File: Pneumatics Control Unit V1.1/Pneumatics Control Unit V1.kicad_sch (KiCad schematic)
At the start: 43 parts

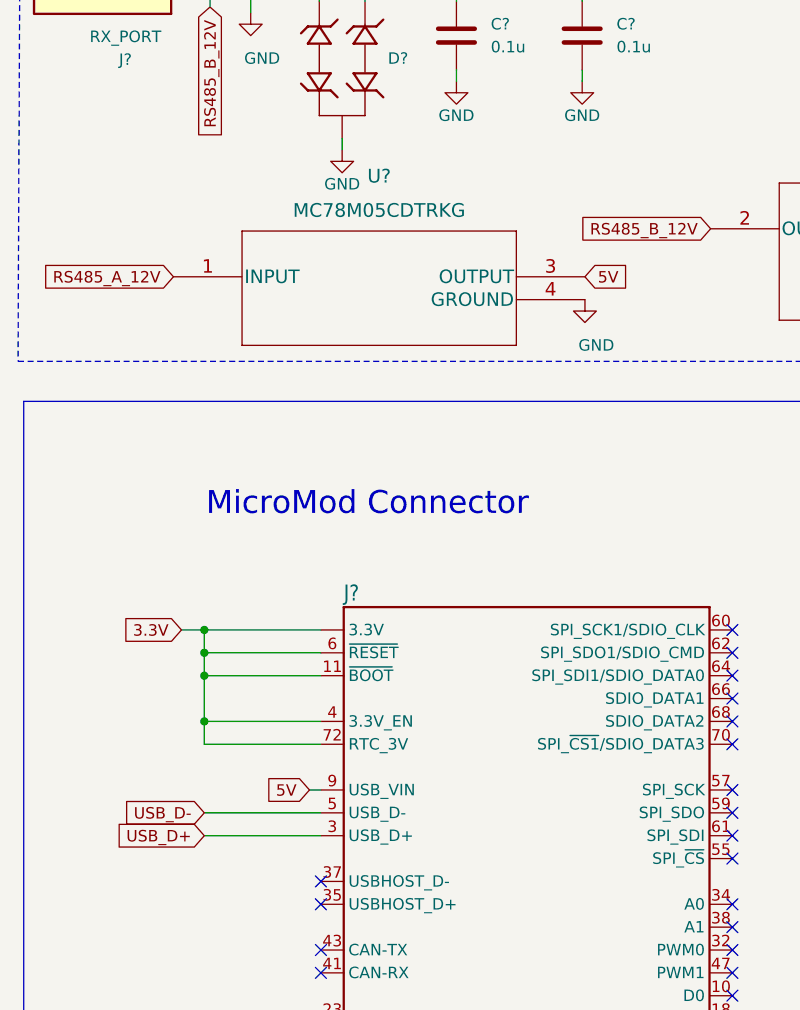
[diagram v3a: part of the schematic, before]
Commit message: Adding voltage converters
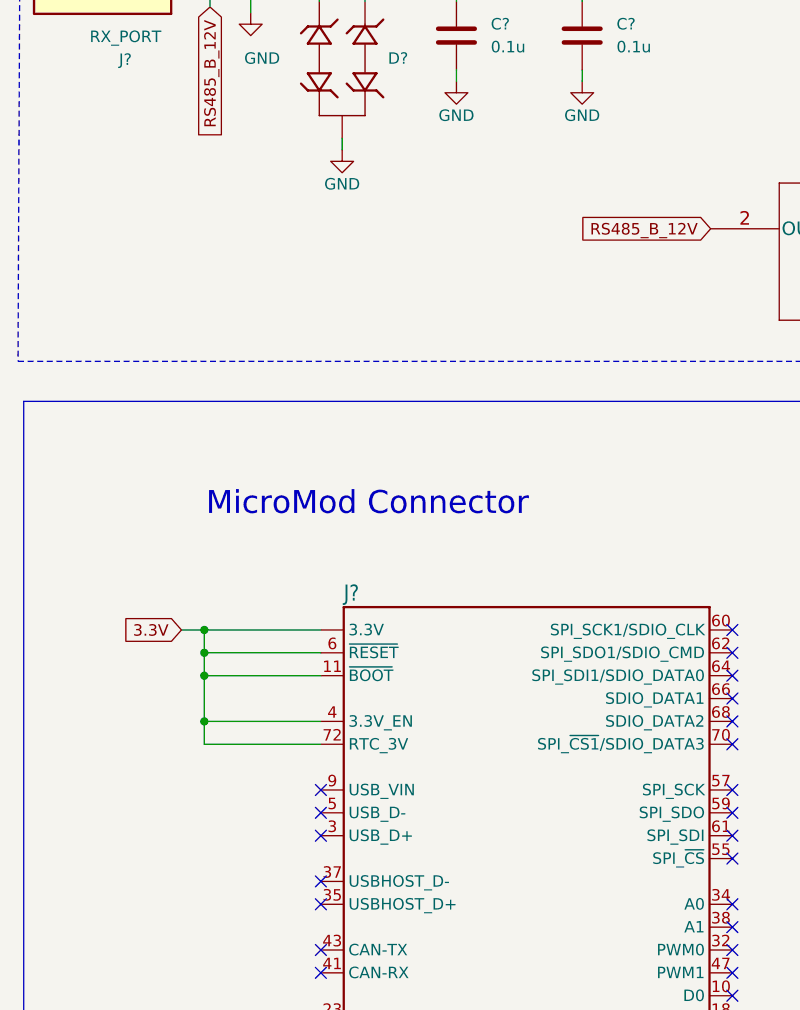
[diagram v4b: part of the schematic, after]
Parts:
- removed U?: MC78M05CDTRKG, DPAK-3_ONS, symbol 2022-03-25_21-05-18:MC78M05CDTRKG
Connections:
- net 5V: no longer names the net of J?.9 (USB_VIN)
- net USB_D+: no longer names the net of J?.3 (USB_D+)
- net USB_D-: no longer names the net of J?.5 (USB_D-)
- no-connect marks 42 -> 45
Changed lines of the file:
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@@
   (no_connect (at 97.155 236.855))
   (no_connect (at 97.155 239.395))
+  (no_connect (at 48.895 163.195))
+  (no_connect (at 48.895 165.735))
+  (no_connect (at 48.895 168.275))
   (no_connect (at 23.495 210.185))
   (no_connect (at 48.895 226.695))
@@
     (stroke (width 0) (type default) (color 0 0 0 0))
   )
-  (wire (pts (xy 35.941 168.275) (xy 48.895 168.275))
-    (stroke (width 0) (type default) (color 0 0 0 0))
-  )
   (wire (pts (xy 104.648 34.3154) (xy 99.5172 34.3154))
     (stroke (width 0) (type default) (color 0 0 0 0))
@@
     (stroke (width 0) (type default) (color 0 0 0 0))
   )
-  (wire (pts (xy 35.941 165.735) (xy 48.895 165.735))
-    (stroke (width 0) (type default) (color 0 0 0 0))
-  )
   (wire (pts (xy 295.91 88.9) (xy 321.31 88.9))
     (stroke (width 0) (type default) (color 0 0 0 0))
@@
   )
   (wire (pts (xy 250.19 52.705) (xy 242.57 52.705))
-    (stroke (width 0) (type default) (color 0 0 0 0))
-  )
-  (wire (pts (xy 47.625 163.195) (xy 48.895 163.195))
     (stroke (width 0) (type default) (color 0 0 0 0))
   )
@@
     )
   )
-  (global_label "USB_D+" (shape input) (at 35.941 168.275 180)
-    (effects (font (size 1.27 1.27)) (justify right))
-    (property "Intersheet References" "${INTERSHEET_REFS}" (id 0) (at 24.3839 168.3544 0)
-      (effects (font (size 1.27 1.27)) (justify right) hide)
-    )
-  )
   (global_label "RS485_RXD" (shape input) (at 128.778 54.61 0)
     (effects (font (size 1.27 1.27)) (justify left))
@@
     )
   )
-  (global_label "RS485_A_12V" (shape input) (at 32.512 106.172 180) (fields_autoplaced)
-    (effects (font (size 1.27 1.27)) (justify right))
-    (property "Intersheet References" "${INTERSHEET_REFS}" (id 0) (at 17.2689 106.0926 0)
-      (effects (font (size 1.27 1.27)) (justify right) hide)
-    )
-  )
   (global_label "3.3V" (shape input) (at 158.242 100.838 0) (fields_autoplaced)
     (effects (font (size 1.27 1.27)) (justify left))
@@
     )
   )
-  (global_label "5V" (shape input) (at 78.232 106.172 0) (fields_autoplaced)
-    (effects (font (size 1.27 1.27)) (justify left))
-    (property "Intersheet References" "${INTERSHEET_REFS}" (id 0) (at 83.1337 106.0926 0)
-      (effects (font (size 1.27 1.27)) (justify left) hide)
-    )
-  )
   (global_label "RS485_TXD" (shape input) (at 129.032 50.292 0)
     (effects (font (size 1.27 1.27)) (justify left))
@@
     )
   )
-  (global_label "USB_D-" (shape input) (at 35.941 165.735 180)
-    (effects (font (size 1.27 1.27)) (justify right))
-    (property "Intersheet References" "${INTERSHEET_REFS}" (id 0) (at 24.3839 165.6556 0)
-      (effects (font (size 1.27 1.27)) (justify right) hide)
-    )
-  )
   (global_label "RS485_TXD" (shape input) (at 148.4376 31.7754 0)
     (effects (font (size 1.27 1.27)) (justify left))
@@
     (effects (font (size 1.27 1.27)) (justify left))
     (property "Intersheet References" "${INTERSHEET_REFS}" (id 0) (at 81.3646 193.5956 0)
-      (effects (font (size 1.27 1.27)) (justify right) hide)
-    )
-  )
-  (global_label "5V" (shape input) (at 47.625 163.195 180) (fields_autoplaced)
-    (effects (font (size 1.27 1.27)) (justify right))
-    (property "Intersheet References" "${INTERSHEET_REFS}" (id 0) (at 42.7233 163.1156 0)
       (effects (font (size 1.27 1.27)) (justify right) hide)
     )
@@
     (pin "2")
     (pin "3")
-  )
-  (symbol (lib_id "power:GND") (at 78.232 108.712 0) (unit 1)
-    (in_bom yes) (on_board yes)
-    (property "Reference" "#PWR?" (id 0) (at 78.232 115.062 0)
-      (effects (font (size 1.27 1.27)) hide)
-    )
-    (property "Value" "GND" (id 1) (at 79.502 113.792 0))
-    (property "Footprint" "" (id 2) (at 78.232 108.712 0)
-      (effects (font (size 1.27 1.27)) hide)
-    )
-    (property "Datasheet" "" (id 3) (at 78.232 108.712 0)
-      (effects (font (size 1.27 1.27)) hide)
-    )
-    (pin "1")
   )
   (symbol (lib_id "Connector:Conn_01x02_Male") (at 260.35 28.575 180) (unit 1)
@@
     (pin "2")
   )
-  (symbol (lib_id "2022-03-25_21-05-18:MC78M05CDTRKG") (at 32.512 106.172 0) (unit 1)
-    (in_bom yes) (on_board yes) (fields_autoplaced)
-    (property "Reference" "U?" (id 0) (at 55.372 94.996 0)
-      (effects (font (size 1.524 1.524)))
-    )
-    (property "Value" "MC78M05CDTRKG" (id 1) (at 55.372 98.806 0)
-      (effects (font (size 1.524 1.524)))
-    )
-    (property "Footprint" "DPAK-3_ONS" (id 2) (at 55.372 100.076 0)
-      (effects (font (size 1.524 1.524)) hide)
-    )
-    (property "Datasheet" "" (id 3) (at 32.512 106.172 0)
-      (effects (font (size 1.524 1.524)))
-    )
-    (pin "1")
-    (pin "3")
-    (pin "4")
-  )
   (symbol (lib_id "power:GND") (at 220.98 53.975 0) (unit 1)
     (in_bom yes) (on_board yes)
@@
       (reference "#PWR?") (unit 1) (value "GND") (footprint "")
     )
-    (path "/907ee120-1742-4b9b-9a3f-9a17112149c4"
-      (reference "#PWR?") (unit 1) (value "GND") (footprint "")
-    )
     (path "/931a035c-dacd-431f-910b-def670bdc676"
       (reference "#PWR?") (unit 1) (value "GND") (footprint "")
@@
       (reference "U?") (unit 1) (value "NCP1117LPST33T3G") (footprint "SOT223-3_ONS")
     )
-    (path "/b9b54933-6106-46ac-bf2e-8b30431ef848"
-      (reference "U?") (unit 1) (value "MC78M05CDTRKG") (footprint "DPAK-3_ONS")
-    )
-  )
+  )

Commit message: Changing to net labels
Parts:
- removed D? (x7): D_TVS_x2_AAC, Package_TO_SOT_SMD:SOT-723, symbol Device:D_TVS_x2_AAC
- removed J? (x7): Conn_01x02_Male, Connector_PinSocket_2.54mm:PinSocket_1x02_P2.54mm_Vertical, symbol Connector:Conn_01x02_Male
- removed MOSFET? (x7): SSM3K7002KFU, footprints:SSM3K7002KFU, symbol 2021-12-24_05-54-00:SSM3K7002KFU
- added D? (x7): D_TVS_x2_AAC, Package_TO_SOT_SMD:SOT-723, symbol Device:D_TVS_x2_AAC
- added J? (x7): Conn_01x02_Male, Connector_PinSocket_2.54mm:PinSocket_1x02_P2.54mm_Vertical, symbol Connector:Conn_01x02_Male
- added MOSFET? (x7): SSM3K7002KFU, footprints:SSM3K7002KFU, symbol 2021-12-24_05-54-00:SSM3K7002KFU
- added U?: MC78M05CDTRKG, DPAK-3_ONS, symbol 2022-03-25_21-05-18:MC78M05CDTRKG
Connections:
- net SIG is gone; now on net GPIO_0: D?.1 (A1)
- net GND: now also D?.3 (common), D?.3 (common), D?.3 (common), D?.3 (common), D?.3 (common), D?.3 (common), D?.3 (common), MOSFET?.2 (SOURCE), MOSFET?.2 (SOURCE), MOSFET?.2 (SOURCE), MOSFET?.2 (SOURCE), MOSFET?.2 (SOURCE), MOSFET?.2 (SOURCE), MOSFET?.2 (SOURCE), U?.4 (GROUND)
- net GPIO_1: now also D?.1 (A1), MOSFET?.1 (GATE)
- net GPIO_2: now also D?.1 (A1), MOSFET?.1 (GATE)
- net GPIO_3: now also D?.1 (A1), MOSFET?.1 (GATE)
- net GPIO_4: now also D?.1 (A1), MOSFET?.1 (GATE)
- net GPIO_5: now also D?.1 (A1), MOSFET?.1 (GATE)
- net GPIO_6: now also D?.1 (A1), MOSFET?.1 (GATE)
- net GPIO_7: now also D?.1 (A1), MOSFET?.1 (GATE)
- net RS485_A_12V: now also U?.1 (INPUT)
- net +5V renamed 5V
- net 5V: now also J?.2 (Pin_2), J?.2 (Pin_2), J?.2 (Pin_2), J?.2 (Pin_2), J?.2 (Pin_2), J?.2 (Pin_2), J?.2 (Pin_2), U?.3 (OUTPUT)
- new net: D?.2 (A2), J?.1 (Pin_1), MOSFET?.3 (DRAIN) (x7)
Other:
- note added: "Pueumatics Control Circuit 4"
- note added: "Pueumatics Control Circuit 5"
- note added: "Pueumatics Control Circuit 6"
- note added: "Pueumatics Control Circuit 7"
- note added: "Pueumatics Control Circuit 8"

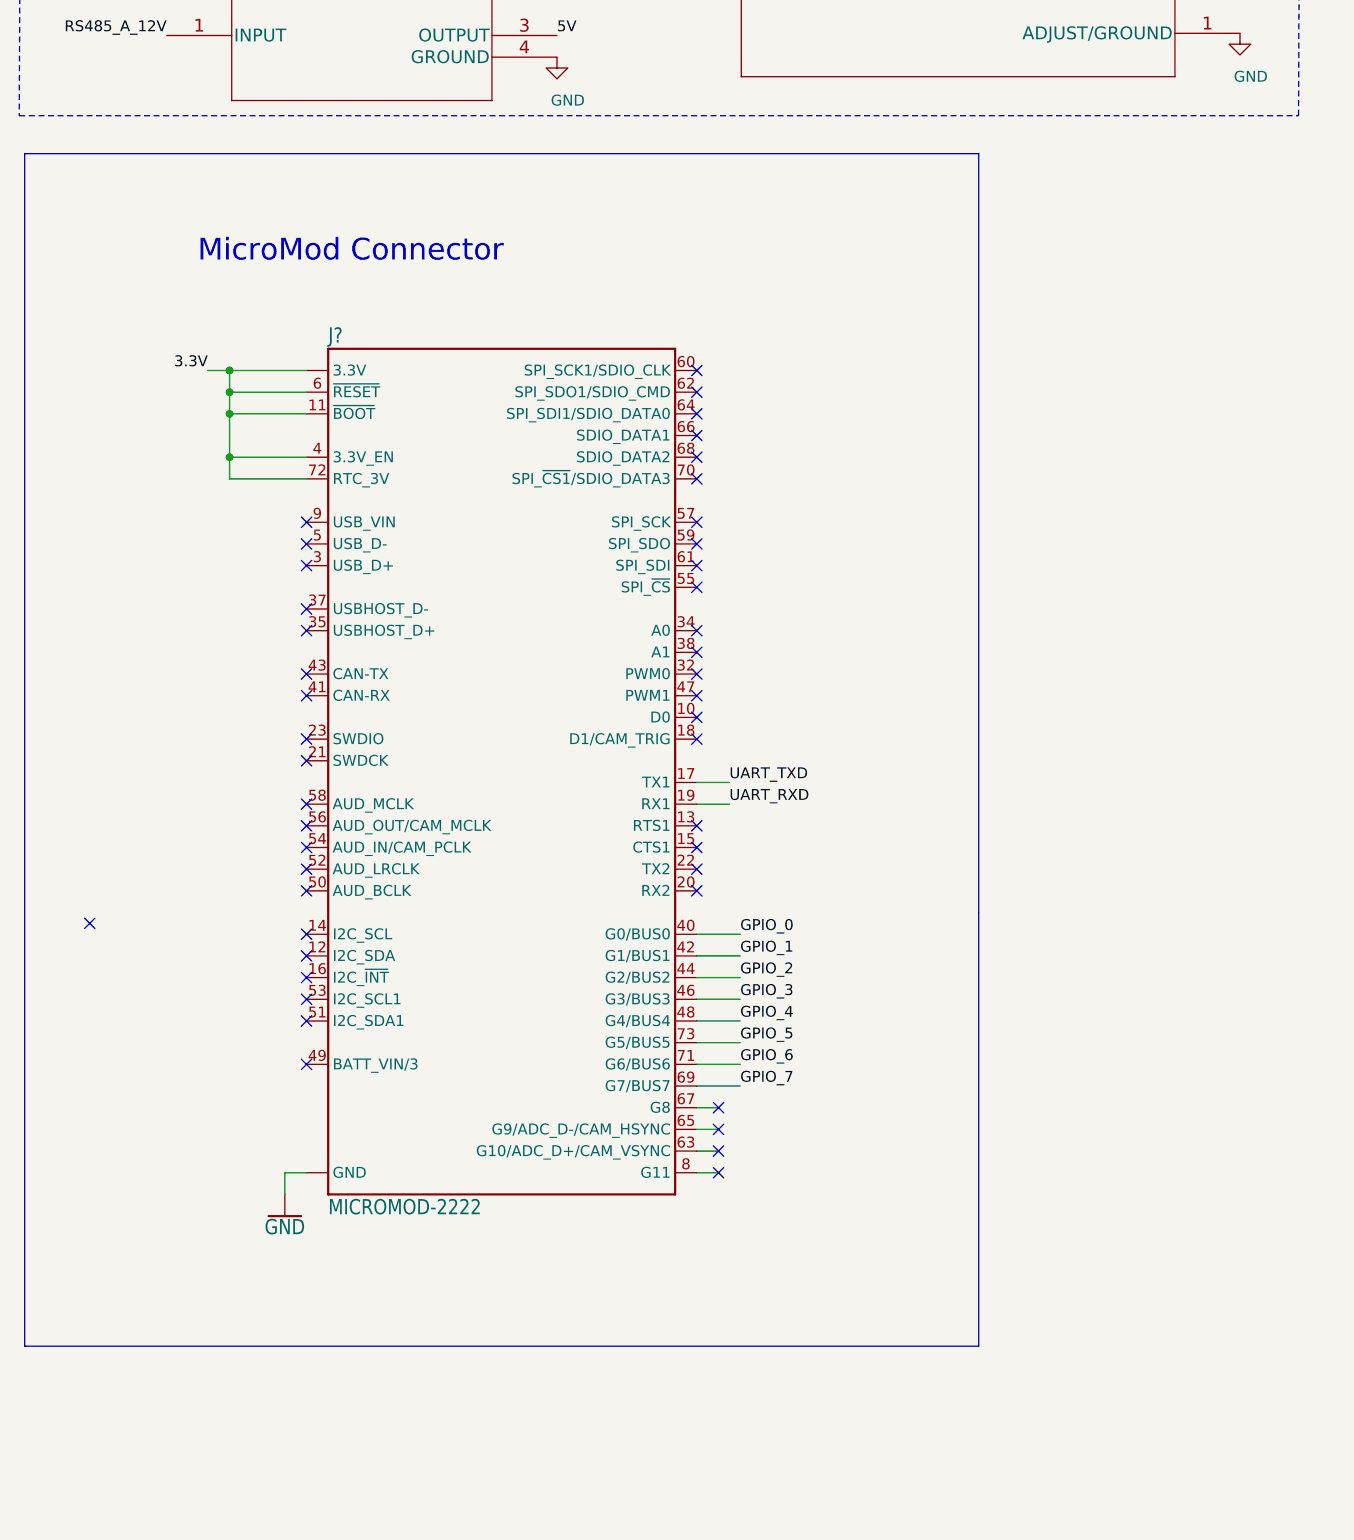
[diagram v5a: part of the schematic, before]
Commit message: Adding m.2
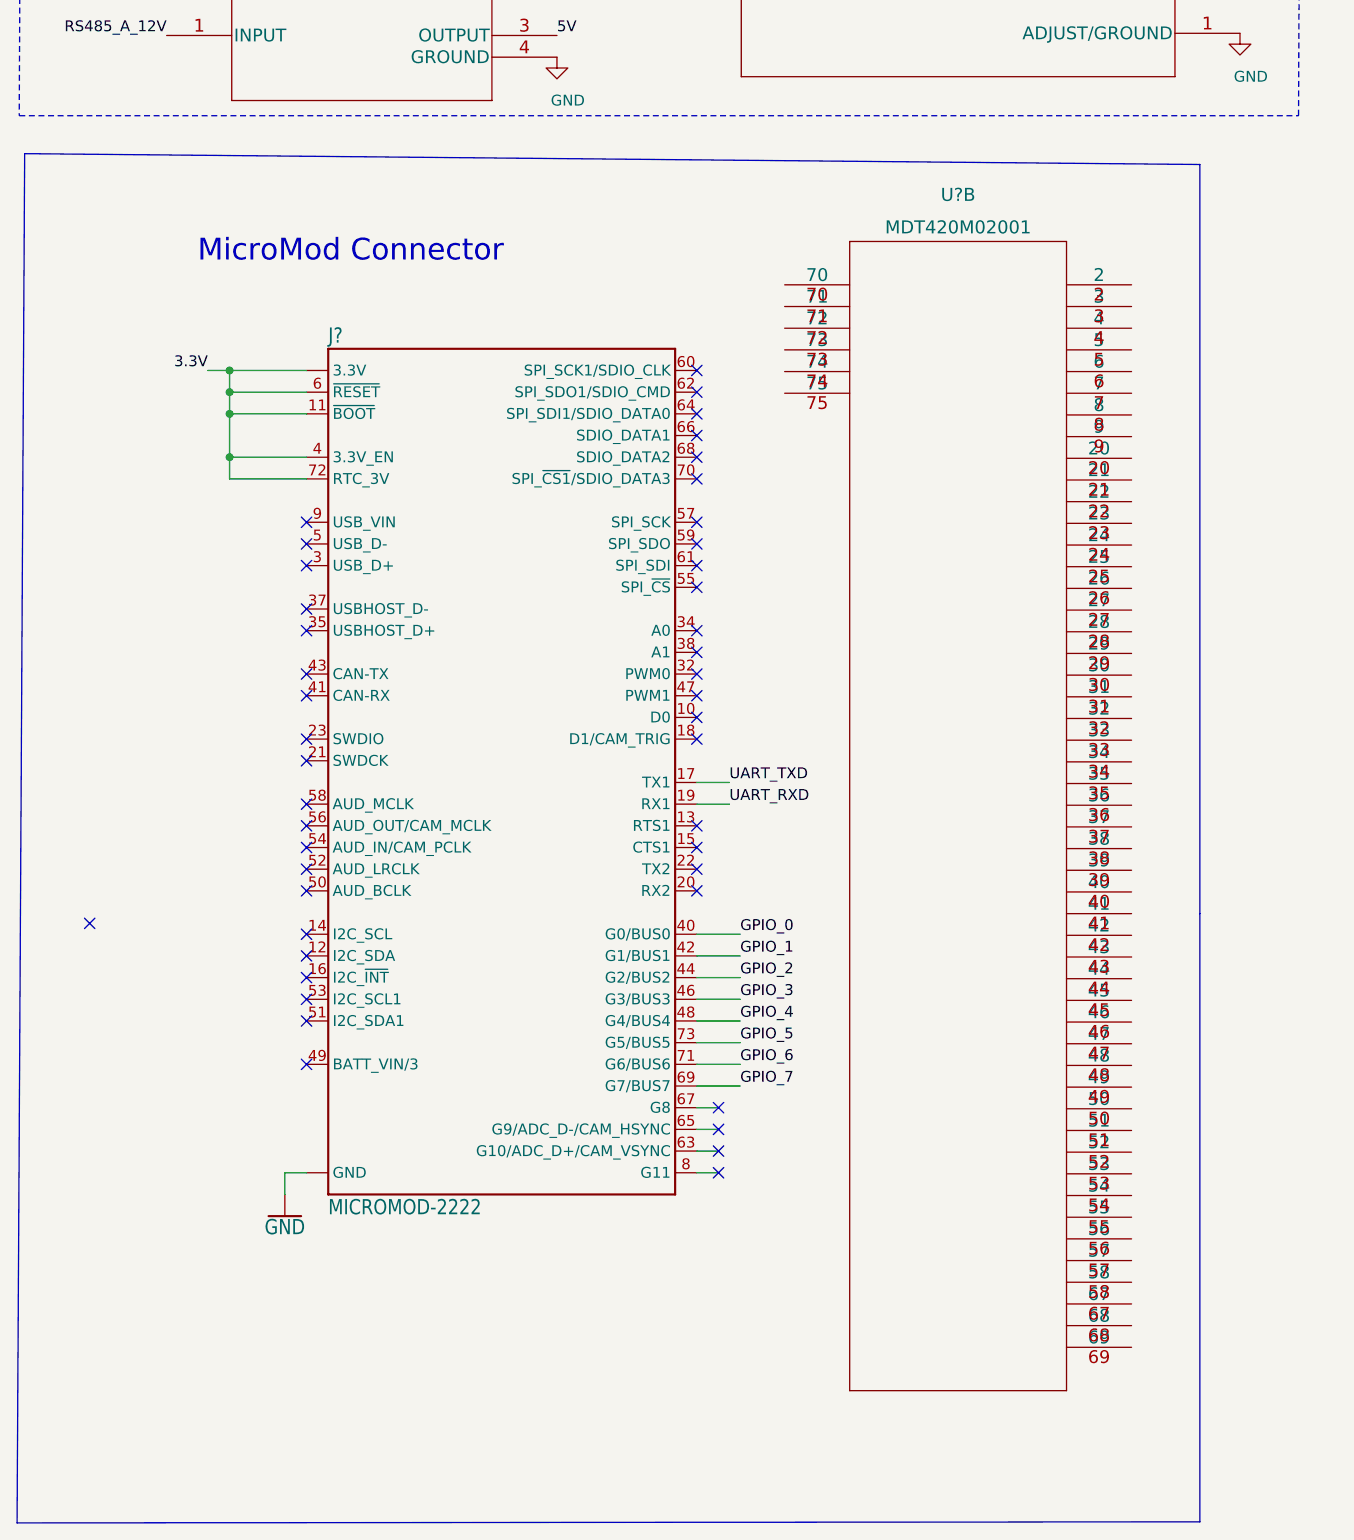
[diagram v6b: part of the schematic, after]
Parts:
- added U?: MDT420M02001, MDT420M02001_AMP, symbol m.2:MDT420M02001
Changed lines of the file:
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@@
     (stroke (width 0) (type default) (color 0 0 0 0))
   )
-  (polyline (pts (xy 127.635 208.915) (xy 127.635 120.015))
+  (polyline (pts (xy 153.543 209.042) (xy 153.543 121.285))
     (stroke (width 0) (type default) (color 0 0 0 0))
   )
@@
     (stroke (width 0) (type default) (color 0 0 0 0))
   )
-  (polyline (pts (xy 127.635 259.715) (xy 15.875 259.715))
+  (polyline (pts (xy 153.543 280.289) (xy 14.986 280.416))
     (stroke (width 0) (type default) (color 0 0 0 0))
   )
@@
     (stroke (width 0) (type default) (color 0 0 0 0))
   )
-  (polyline (pts (xy 15.875 120.015) (xy 15.875 259.715))
+  (polyline (pts (xy 15.875 120.015) (xy 14.986 280.416))
     (stroke (width 0) (type default) (color 0 0 0 0))
   )
@@
     (stroke (width 0) (type solid) (color 0 0 0 0))
   )
-  (polyline (pts (xy 15.875 120.015) (xy 127.635 120.015))
+  (polyline (pts (xy 15.875 120.015) (xy 153.543 121.285))
     (stroke (width 0) (type default) (color 0 0 0 0))
   )
@@
     (stroke (width 0) (type default) (color 0 0 0 0))
   )
-  (polyline (pts (xy 127.635 259.715) (xy 127.635 208.915))
+  (polyline (pts (xy 153.543 280.289) (xy 153.543 209.042))
     (stroke (width 0) (type default) (color 0 0 0 0))
   )
@@
     (pin "1")
   )
+  (symbol (lib_id "m.2:MDT420M02001") (at 145.542 135.382 0) (mirror y) (unit 2)
+    (in_bom yes) (on_board yes) (fields_autoplaced)
+    (property "Reference" "U?" (id 0) (at 125.222 124.841 0)
+      (effects (font (size 1.524 1.524)))
+    )
+    (property "Value" "MDT420M02001" (id 1) (at 125.222 128.651 0)
+      (effects (font (size 1.524 1.524)))
+    )
+    (property "Footprint" "MDT420M02001_AMP" (id 2) (at 165.862 126.746 0)
+      (effects (font (size 1.524 1.524)) hide)
+    )
+    (property "Datasheet" "" (id 3) (at 145.542 135.382 0)
+      (effects (font (size 1.524 1.524)))
+    )
+    (pin "2")
+    (pin "20")
+    (pin "21")
+    (pin "22")
+    (pin "23")
+    (pin "24")
+    (pin "25")
+    (pin "26")
+    (pin "27")
+    (pin "28")
+    (pin "29")
+    (pin "3")
+    (pin "30")
+    (pin "31")
+    (pin "32")
+    (pin "33")
+    (pin "34")
+    (pin "35")
+    (pin "36")
+    (pin "37")
+    (pin "38")
+    (pin "39")
+    (pin "4")
+    (pin "40")
+    (pin "41")
+    (pin "42")
+    (pin "43")
+    (pin "44")
+    (pin "45")
+    (pin "46")
+    (pin "47")
+    (pin "48")
+    (pin "49")
+    (pin "5")
+    (pin "50")
+    (pin "51")
+    (pin "52")
+    (pin "53")
+    (pin "54")
+    (pin "55")
+    (pin "56")
+    (pin "57")
+    (pin "58")
+    (pin "6")
+    (pin "67")
+    (pin "68")
+    (pin "69")
+    (pin "7")
+    (pin "70")
+    (pin "71")
+    (pin "72")
+    (pin "73")
+    (pin "74")
+    (pin "75")
+    (pin "8")
+    (pin "9")
+  )
   (symbol (lib_id "power:GND") (at 221.107 145.542 0) (unit 1)
     (in_bom yes) (on_board yes)
@@
       (reference "U?") (unit 1) (value "MC78M05CDTRKG") (footprint "DPAK-3_ONS")
     )
-  )
+    (path "/a0fc109e-39e3-4b9b-bb0a-dce49a5ef63b"
+      (reference "U?") (unit 2) (value "MDT420M02001") (footprint "MDT420M02001_AMP")
+    )
+  )
